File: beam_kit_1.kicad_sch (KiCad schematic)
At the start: 26 parts, among them J1 PZ2.54-2*20, J2 PZ2.54-2*20, SW3 RUN

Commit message: fit test
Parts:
- removed SW3: RUN, Button_Switch_SMD:SW_Push_1P1T_NO_6x6mm_H9.5mm, symbol Switch:SW_Push
- added J10: UART_SEPARATOR, Connector_PinHeader_2.54mm:PinHeader_2x02_P2.54mm_Vertical, symbol Connector_Generic:Conn_02x02_Odd_Even
- added J15, J16, J17, J18: dbg, Connector_JST:JST_SH_BM03B-SRSS-TB_1x03-1MP_P1.00mm_Vertical, symbol Connector_Generic:Conn_01x03
- added SW7: RUN, Button_Switch_SMD:SW_SPST_B3U-1000P, symbol Switch:SW_Push
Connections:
- net GND: now also J15.2 (Pin_2), J16.2 (Pin_2), J17.2 (Pin_2), J18.2 (Pin_2), SW7.1
- net GPIO0: now also J10.4 (Pin_4)
- net GPIO1: now also J10.2 (Pin_2)
- net SWCLK: now also J15.1 (Pin_1), J17.3 (Pin_3)
- net SWDIO: now also J15.3 (Pin_3), J17.1 (Pin_1)
- net prog/TARGET_RX: now also J10.1 (Pin_1), J16.1 (Pin_1), J18.3 (Pin_3)
- net prog/TARGET_TX: now also J10.3 (Pin_3), J16.3 (Pin_3), J18.1 (Pin_1)
- net at A1.30 (RUN), R12.1: now also SW7.2

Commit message: layout
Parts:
- added H1, H2, H3, H4, H5: Hole, MountingHole:MountingHole_3.2mm_M3_Pad_Via, symbol Mechanical:MountingHole_Pad
- added H6: MB template, MountingHole:MountingHole_2.1mm, symbol Mechanical:MountingHole
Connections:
- net GND: now also H1.1, H2.1, H3.1, H4.1, H5.1

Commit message: layout
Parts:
- added H7: Hole, MountingHole:MountingHole_3.2mm_M3_Pad_Via, symbol Mechanical:MountingHole_Pad
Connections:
- net GND: now also H7.1
- net GPIO0: now also J10.2 (Pin_2); no longer J10.4 (Pin_4)
- net GPIO1: now also J10.4 (Pin_4); no longer J10.2 (Pin_2)
- net prog/TARGET_RX: now also J10.3 (Pin_3); no longer J10.1 (Pin_1)
- net prog/TARGET_TX: now also J10.1 (Pin_1); no longer J10.3 (Pin_3)
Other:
- note added: "TODO: Add 3V3 regulator"
- moved on the sheet: A1, H6, R12, SW7

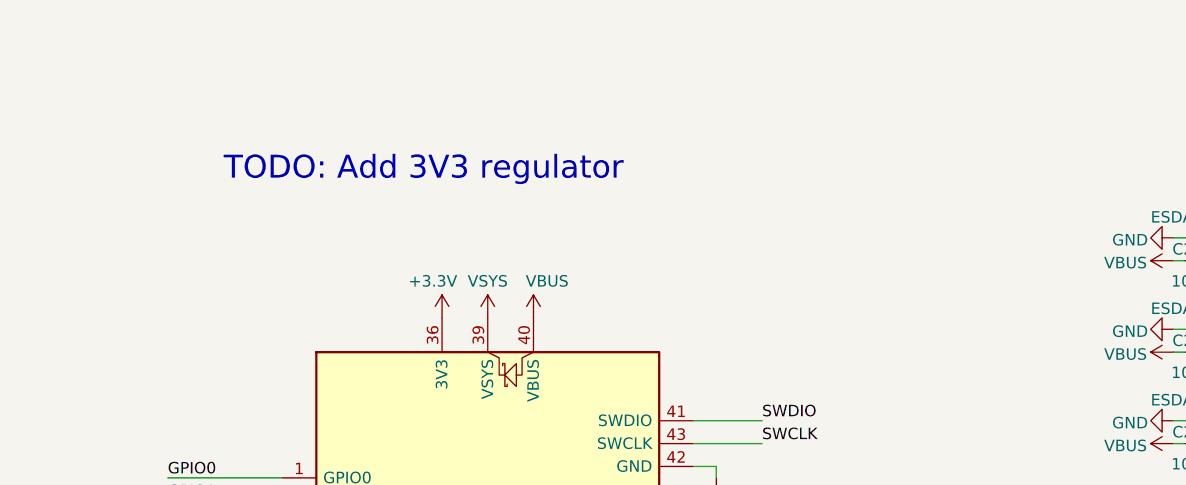
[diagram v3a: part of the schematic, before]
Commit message: preparing for more modules
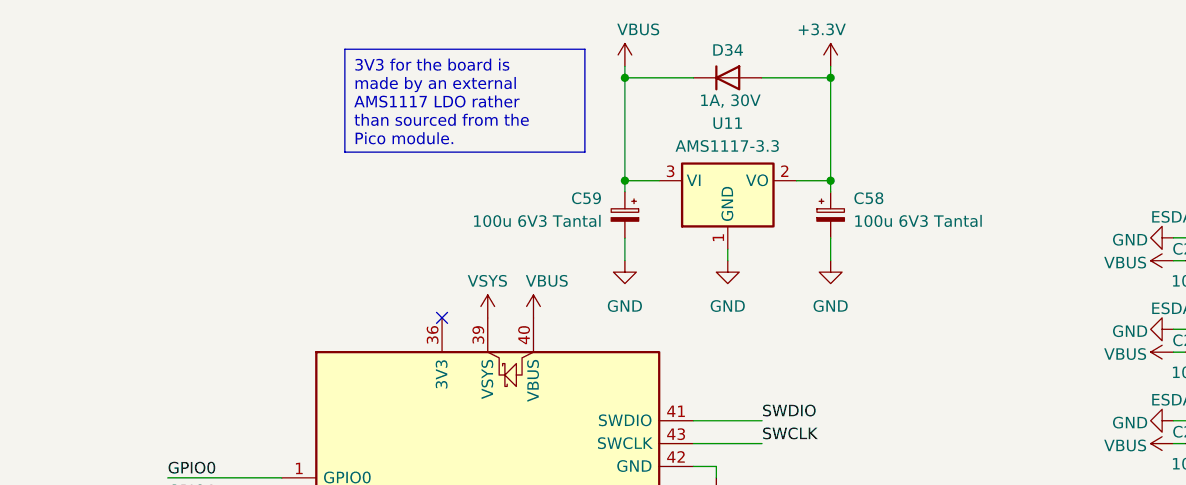
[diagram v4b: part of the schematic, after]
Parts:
- added C58, C59: 100u 6V3 Tantal, Capacitor_Tantalum_SMD:CP_EIA-3528-21_Kemet-B_Pad1.50x2.35mm_HandSolder, symbol Device:C_Polarized_Small
- added D34: 1A, 30V, Diode_SMD:D_PowerDI-123, symbol Device:D
- added U11: AMS1117-3.3, Package_TO_SOT_SMD:SOT-223-3_TabPin2, symbol Regulator_Linear:AMS1117-3.3
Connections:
- net +3.3V: now also C58.1, D34.2 (A), U11.2 (VO); no longer A1.36 (3V3)
- net GND: now also C58.2, C59.2, U11.1 (GND)
- net VBUS: now also C59.1, D34.1 (K), U11.3 (VI)
- no-connect marks 6 -> 7
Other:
- note removed: "TODO: Add 3V3 regulator"

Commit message: more stuff added to sch
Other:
- added sheet peripheral2 (peripheral2.kicad_sch)
- moved on the sheet: J10, J15, J16, J17, J18

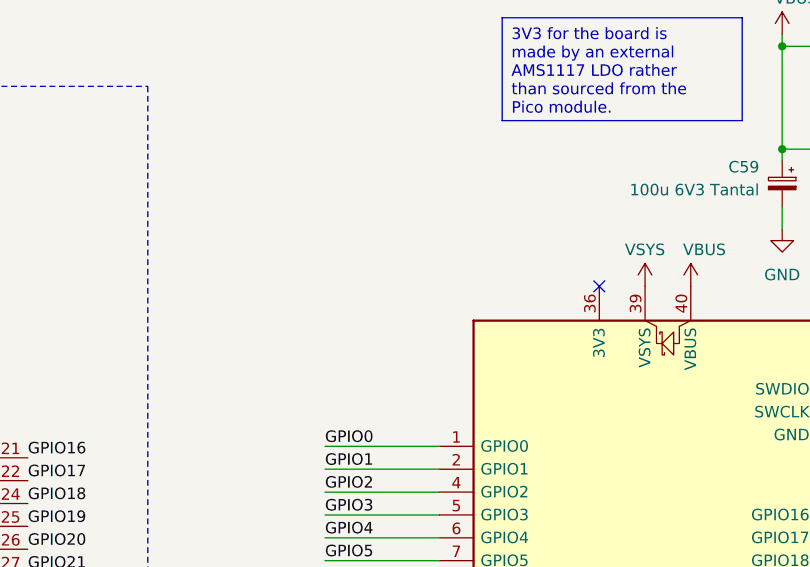
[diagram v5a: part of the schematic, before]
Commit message: kju fix and PCB size increase
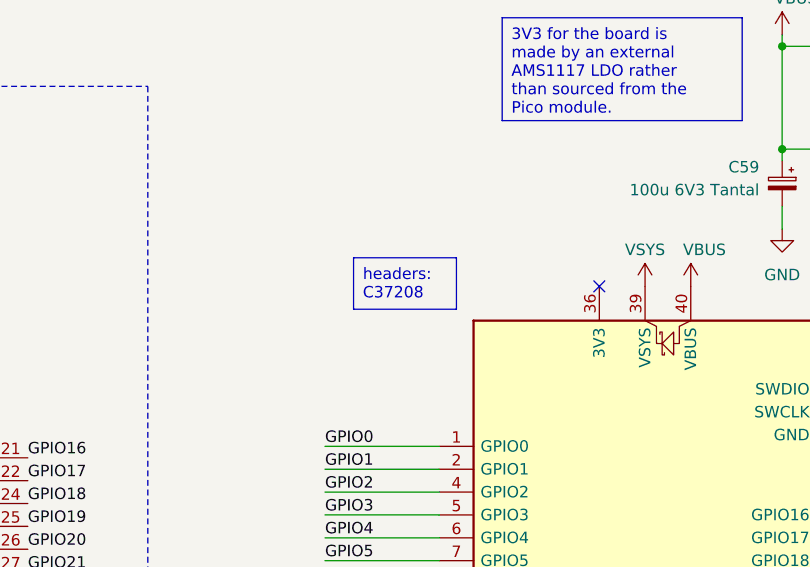
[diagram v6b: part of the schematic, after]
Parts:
- A1: now left out of the parts list
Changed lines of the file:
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@@
+		)
+	)
+	(text_box "headers: \nC37208"
+		(exclude_from_sim no)
+		(at 112.395 45.085 0)
+		(size 11.43 5.715)
+		(stroke
+			(width 0)
+			(type default)
+		)
+		(fill
+			(type none)
+		)
+		(effects
+			(font
+				(size 1.27 1.27)
+			)
+			(justify left top)
 		)
 	)
@@
 		(unit 1)
 		(exclude_from_sim no)
-		(in_bom yes)
+		(in_bom no)
 		(on_board yes)
 		(dnp no)

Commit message: layout
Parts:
- added H8: Hole, MountingHole:MountingHole_3.2mm_M3_Pad_Via, symbol Mechanical:MountingHole_Pad
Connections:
- net +3.3V: no longer D5.1 (TVS1), J2.10 (Pin_10), J2.9 (Pin_9)
- net GND: now also H8.1
- new net: D5.1 (TVS1), J2.10 (Pin_10), J2.9 (Pin_9)
- no-connect marks 7 -> 8
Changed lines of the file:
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@@
 	)
 	(junction
+		(at 257.81 45.72)
+		(diameter 0)
+		(color 0 0 0 0)
+	)
+	(junction
 		(at 257.81 55.88)
 		(diameter 0)
@@
 	)
 	(junction
-		(at 257.81 45.72)
-		(diameter 0)
-		(color 0 0 0 0)
-	)
-	(junction
 		(at 245.11 121.92)
 		(diameter 0)
@@
 	)
 	(no_connect
+		(at 259.08 45.72)
+	)
+	(no_connect
 		(at 30.48 105.41)
 	)
@@
 	(wire
 		(pts
-			(xy 280.67 48.26) (xy 270.51 48.26)
-		)
-		(stroke
-			(width 0)
-			(type default)
-		)
-	)
-	(wire
-		(pts
 			(xy 257.81 99.06) (xy 271.78 99.06)
 		)
@@
 	(wire
 		(pts
+			(xy 257.81 45.72) (xy 259.08 45.72)
+		)
+		(stroke
+			(width 0)
+			(type default)
+		)
+	)
+	(wire
+		(pts
 			(xy 228.6 72.39) (xy 228.6 69.85)
 		)
@@
 	(wire
 		(pts
-			(xy 257.81 45.72) (xy 270.51 45.72)
-		)
-		(stroke
-			(width 0)
-			(type default)
-		)
-	)
-	(wire
-		(pts
 			(xy 167.64 83.82) (xy 175.26 83.82)
 		)
@@
 	(wire
 		(pts
-			(xy 280.67 43.18) (xy 280.67 48.26)
-		)
-		(stroke
-			(width 0)
-			(type default)
-		)
-	)
-	(wire
-		(pts
 			(xy 271.78 111.76) (xy 271.78 113.03)
 		)
@@
 	(wire
 		(pts
-			(xy 270.51 45.72) (xy 270.51 48.26)
-		)
-		(stroke
-			(width 0)
-			(type default)
-		)
-	)
-	(wire
-		(pts
 			(xy 275.59 33.02) (xy 275.59 38.1)
 		)
@@
 	)
 	(symbol
+		(lib_id "Mechanical:MountingHole_Pad")
+		(at 232.41 154.94 0)
+		(unit 1)
+		(exclude_from_sim yes)
+		(in_bom no)
+		(on_board yes)
+		(dnp no)
+		(fields_autoplaced yes)
+		(property "Reference" "H8"
+			(at 234.95 152.3999 0)
+			(effects
+				(font
+					(size 1.27 1.27)
+				)
+				(justify left)
+			)
+		)
+		(property "Value" "Hole"
+			(at 234.95 154.9399 0)
+			(effects
+				(font
+					(size 1.27 1.27)
+				)
+				(justify left)
+			)
+		)
+		(property "Footprint" "MountingHole:MountingHole_3.2mm_M3_Pad_Via"
+			(at 232.41 154.94 0)
+			(effects
+				(font
+					(size 1.27 1.27)
+				)
+				(hide yes)
+			)
+		)
+		(property "Datasheet" "~"
+			(at 232.41 154.94 0)
+			(effects
+				(font
+					(size 1.27 1.27)
+				)
+				(hide yes)
+			)
+		)
+		(property "Description" "Mounting Hole with connection"
+			(at 232.41 154.94 0)
+			(effects
+				(font
+					(size 1.27 1.27)
+				)
+				(hide yes)
+			)
+		)
+		(pin "1"
+		)
+		(instances
+			(project "beam_kit_1"
+				(path "/3a707576-1044-44db-8cf8-deb84fe605c8"
+					(reference "H8")
+					(unit 1)
+				)
+			)
+		)
+	)
+	(symbol
 		(lib_id "Device:D")
 		(at 171.45 21.59 0)
@@
 	)
 	(symbol
+		(lib_id "power:GND")
+		(at 232.41 157.48 0)
+		(unit 1)
+		(exclude_from_sim no)
+		(in_bom yes)
+		(on_board yes)
+		(dnp no)
+		(fields_autoplaced yes)
+		(property "Reference" "#PWR0233"
+			(at 232.41 163.83 0)
+			(effects
+				(font
+					(size 1.27 1.27)
+				)
+				(hide yes)
+			)
+		)
+		(property "Value" "GND"
+			(at 232.41 162.56 0)
+			(effects
+				(font
+					(size 1.27 1.27)
+				)
+			)
+		)
+		(property "Footprint" ""
+			(at 232.41 157.48 0)
+			(effects
+				(font
+					(size 1.27 1.27)
+				)
+				(hide yes)
+			)
+		)
+		(property "Datasheet" ""
+			(at 232.41 157.48 0)
+			(effects
+				(font
+					(size 1.27 1.27)
+				)
+				(hide yes)
+			)
+		)
+		(property "Description" "Power symbol creates a global label with name \"GND\" , ground"
+			(at 232.41 157.48 0)
+			(effects
+				(font
+					(size 1.27 1.27)
+				)
+				(hide yes)
+			)
+		)
+		(pin "1"
+		)
+		(instances
+			(project "beam_kit_1"
+				(path "/3a707576-1044-44db-8cf8-deb84fe605c8"
+					(reference "#PWR0233")
+					(unit 1)
+				)
+			)
+		)
+	)
+	(symbol
 		(lib_id "power:VCC")
 		(at 144.78 48.26 0)
@@
 					(unit 1)
 				)
-			)
-		)
-	)
-	(symbol
-		(lib_id "power:+3.3V")
-		(at 280.67 43.18 0)
-		(unit 1)
-		(exclude_from_sim no)
-		(in_bom yes)
-		(on_board yes)
-		(dnp no)
-		(fields_autoplaced yes)
-		(property "Reference" "#PWR08"
-			(at 280.67 46.99 0)
-			(effects
-				(font
-					(size 1.27 1.27)
-				)
-				(hide yes)
-			)
-		)
-		(property "Value" "+3.3V"
-			(at 280.67 38.1 0)
-			(effects
-				(font
-					(size 1.27 1.27)
-				)
-			)
-		)
-		(property "Footprint" ""
-			(at 280.67 43.18 0)
-			(effects
-				(font
-					(size 1.27 1.27)
-				)
-				(hide yes)
-			)
-		)
-		(property "Datasheet" ""
-			(at 280.67 43.18 0)
-			(effects
-				(font
-					(size 1.27 1.27)
-				)
-				(hide yes)
-			)
-		)
-		(property "Description" "Power symbol creates a global label with name \"+3.3V\""
-			(at 280.67 43.18 0)
-			(effects
-				(font
-					(size 1.27 1.27)
-				)
-				(hide yes)
-			)
-		)
-		(pin "1"
-		)
-		(instances
-			(project ""
-				(path "/3a707576-1044-44db-8cf8-deb84fe605c8"
-					(reference "#PWR08")
-					(unit 1)
-				)

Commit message: layout
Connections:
- net VREF: now reaches D5.3 (TVS2), J2.11 (Pin_11), J2.12 (Pin_12)
- net VREF: now also A1.35 (ADC_VREF), A2.35 (ADC_VREF)
- no-connect marks 8 -> 5
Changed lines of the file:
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@@
-	)
-	(no_connect
-		(at 76.2 87.63)
 	)
 	(no_connect
@@
 	)
 	(no_connect
-		(at 167.64 93.98)
-	)
-	(no_connect
 		(at 259.08 43.18)
-	)
-	(no_connect
-		(at 259.08 48.26)
 	)
 	(no_connect
@@
 		(pts
 			(xy 121.92 158.75) (xy 133.35 158.75)
+		)
+		(stroke
+			(width 0)
+			(type default)
+		)
+	)
+	(wire
+		(pts
+			(xy 167.64 93.98) (xy 175.26 93.98)
 		)
 		(stroke
@@
 		)
 	)
+	(label "VREF"
+		(at 175.26 93.98 0)
+		(fields_autoplaced yes)
+		(effects
+			(font
+				(size 1.27 1.27)
+			)
+			(justify left bottom)
+		)
+	)
 	(label "GPIO20"
 		(at 259.08 71.12 0)
@@
 		)
 	)
+	(label "VREF"
+		(at 76.2 87.63 0)
+		(fields_autoplaced yes)
+		(effects
+			(font
+				(size 1.27 1.27)
+			)
+			(justify left bottom)
+		)
+	)
 	(label "GPIO20"
 		(at 175.26 83.82 0)
@@
 		(fields_autoplaced yes)
 		(effects
+			(font
+				(size 1.27 1.27)
+			)
+			(justify left bottom)
+		)
+	)
+	(label "VREF"
+		(at 259.08 48.26 0)
+		(fields_autoplaced yes)
+		(effects
